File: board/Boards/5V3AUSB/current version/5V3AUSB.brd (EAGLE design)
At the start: 45.7 x 41.6 mm, 14 parts

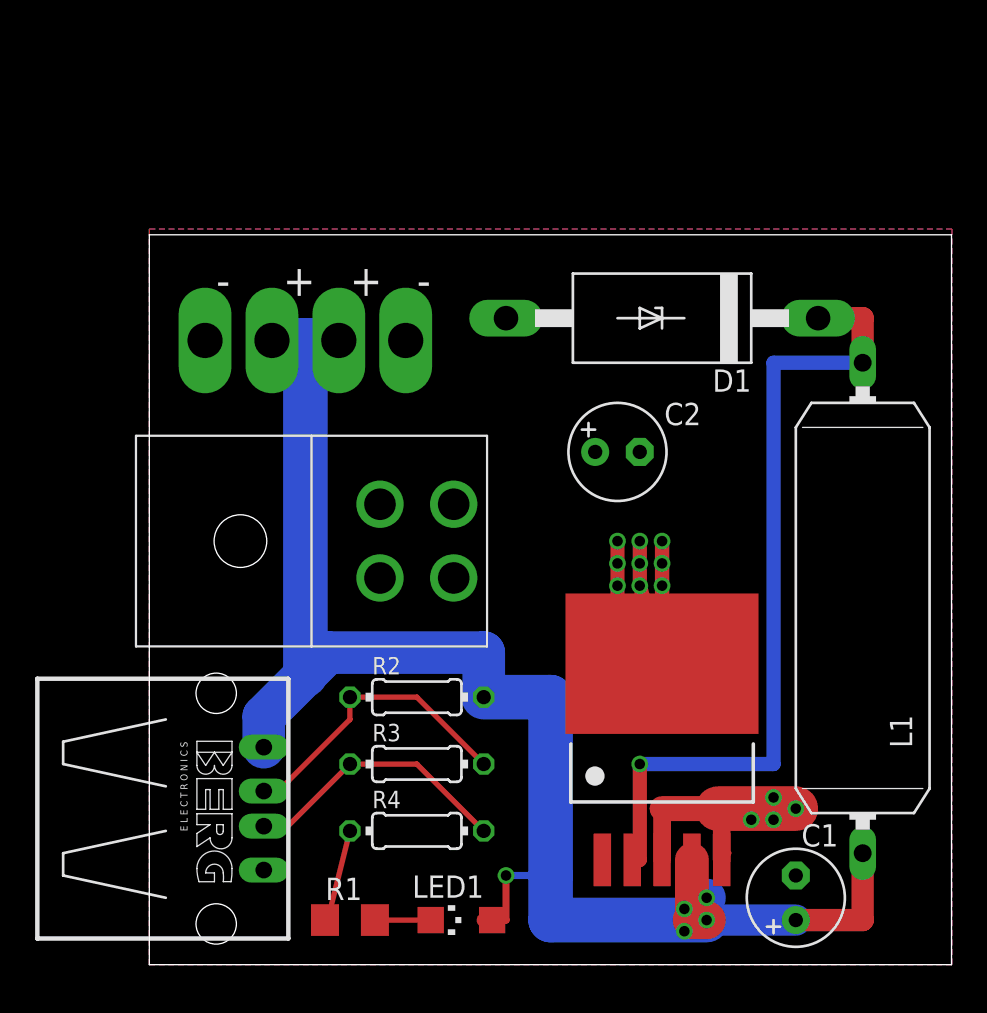
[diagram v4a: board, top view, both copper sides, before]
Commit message: added new board, complete revision of everything
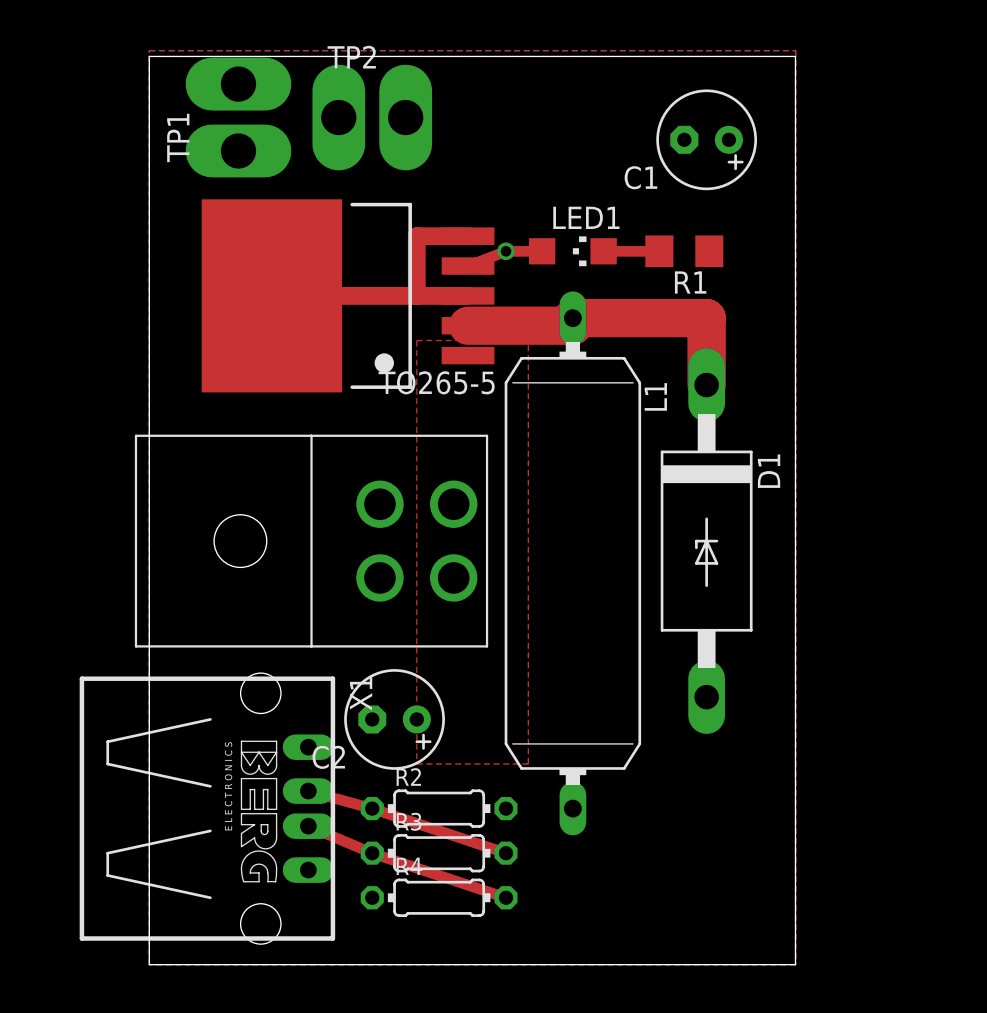
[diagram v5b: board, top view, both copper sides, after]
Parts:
- moved C1 43.5 mm to (31.8, 47.0), turned to 180 degrees
- moved R1 42.6 mm to (30.5, 40.6), turned to 180 degrees
- moved LED1 38.6 mm to (24.1, 40.6), turned to 270 degrees
- moved TO265-5 30.7 mm to (10.2, 38.1), turned to 90 degrees
- moved C2 19.8 mm to (14.0, 14.0), turned to 180 degrees
- moved L1 16.7 mm to (24.1, 22.9)
- moved D1 13.0 mm to (31.8, 24.1), turned to 270 degrees
- moved TP1 12.7 mm to (5.08, 48.3), turned to 90 degrees
- moved TP2 12.7 mm to (12.7, 48.3)
- moved R2 6.48 mm to (16.5, 8.89)
- moved R3 5.24 mm to (16.5, 6.35)
- moved R4 4.02 mm to (16.5, 3.81)
- moved X1 2.54 mm to (6.35, 8.89)
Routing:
- net N$3: track 91.8 -> 4.38 mm, vias 2 -> 1
- net N$2: track 46.5 -> 17.8 mm, vias 1 -> 0
- net GND: track 39.5 -> 17.5 mm, vias 13 -> 0
- net N$7: track 17.0 -> 11.8 mm
- net N$6: track 15.7 -> 12.0 mm
- net N$8: track 0.64 -> 0.00 mm, vias 1 -> 0
- net N$5: track 3.81 -> 3.18 mm
- added copper zone on layer 1, net GND
- added copper zone on layer 16, net N$3
- removed copper zone on layer 16, net GND
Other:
- board size 45.7 x 41.6 mm -> 36.8 x 51.7 mm
- board text removed: "+"
- board text removed: "-"
- board text removed: "5V 3A USB Supply v1.0 C.G & D.K hitchBOT - August 2014"
